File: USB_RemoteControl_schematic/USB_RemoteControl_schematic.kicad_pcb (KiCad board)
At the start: 2 copper layers, 82 x 20 mm, 33 parts, among them J1 USB_A, J2 FOUR_WIRE_CONN, SW1 ~rst, SW2 boot, U1 AMS1117-3.3, U2 STM32F103C6Tx, U3 NRF24L01_Breakout, Y1 8MHz

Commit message: Finished PCB
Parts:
- removed JP1: OPT_0, Resistor_SMD:R_0805_2012Metric_Pad1.20x1.40mm_HandSolder
- removed JP2: OPT_1, Resistor_SMD:R_0805_2012Metric_Pad1.20x1.40mm_HandSolder
- removed JP3: OPT_2, Resistor_SMD:R_0805_2012Metric_Pad1.20x1.40mm_HandSolder
- removed JP4: OPT_3, Resistor_SMD:R_0805_2012Metric_Pad1.20x1.40mm_HandSolder
- removed JP5: OPT_4, Resistor_SMD:R_0805_2012Metric_Pad1.20x1.40mm_HandSolder
- removed JP6: OPT_5, Resistor_SMD:R_0805_2012Metric_Pad1.20x1.40mm_HandSolder
- removed JP7: OPT_6, Resistor_SMD:R_0805_2012Metric_Pad1.20x1.40mm_HandSolder
- removed JP8: OPT_7, Resistor_SMD:R_0805_2012Metric_Pad1.20x1.40mm_HandSolder
- added D3: Green, LED_SMD:LED_0805_2012Metric_Pad1.15x1.40mm_HandSolder, F.Cu at (137.0, 118.3)
- added D4: Blue, LED_SMD:LED_0805_2012Metric_Pad1.15x1.40mm_HandSolder, F.Cu at (141.5, 118.3)
- added R7: 1K, Resistor_SMD:R_0805_2012Metric_Pad1.20x1.40mm_HandSolder, F.Cu at (134.8, 118.2)
- added R8: 1K, Resistor_SMD:R_0805_2012Metric_Pad1.20x1.40mm_HandSolder, F.Cu at (139.2, 118.2)
- added SW3: ~, custom_buttons_switches:TSB008, F.Cu at (135.2, 127.0)
- added SW4: ~, custom_buttons_switches:TSB008, F.Cu at (139.2, 127.0)
- C1, C2: footprint Capacitor_SMD:C_1206_3216Metric_Pad1.33x1.80mm_HandSolder -> Capacitor_SMD:C_0805_2012Metric_Pad1.18x1.45mm_HandSolder; moved to B.Cu
- C3, J2, R1, R2, R3, R5: moved to B.Cu
- D1, D2: footprint LED_SMD:LED_1206_3216Metric_Pad1.42x1.75mm_HandSolder -> LED_SMD:LED_0805_2012Metric_Pad1.15x1.40mm_HandSolder
- J1: footprint Connector_USB:USB_A_CONNFLY_DS1095-WNR0 -> Connectors_Custom:USB_A_Male
- R4: value 220R -> 1K; moved to B.Cu
- R6: value 220R -> 1K
- U1: value AMS1117-3.3 -> HT7533; footprint Package_TO_SOT_SMD:SOT-223-3_TabPin2 -> Package_TO_SOT_SMD:SOT-89-3; moved to B.Cu
- U3: value NRF24L01_Breakout -> JDY-33; footprint RF_Module:nRF24L01_Breakout -> Bluetooth_Custom:JDY-33, JDY-32, JDY-31, JDY-30, JDY-09
- Y1: footprint Crystal:Crystal_SMD_HC49-SD_HandSoldering -> Crystal:Crystal_SMD_HC49-SD
- moved SW2 81.1 mm to (130.8, 133.0), turned to 90 degrees
- moved C1 78.6 mm to (109.5, 129.0), turned to 270 degrees
- moved J2 77.2 mm to (111.0, 133.0), turned to 270 degrees
- moved R6 75.3 mm to (128.0, 118.2), turned to 270 degrees
- moved U1 73.1 mm to (113.5, 128.2), turned to 0 degrees
- moved J1 72.5 mm to (100.0, 125.0)
- moved R2 72.4 mm to (113.8, 122.3)
- moved SW1 71.5 mm to (131.2, 127.0)
- moved D2 71.5 mm to (130.2, 118.2), turned to 270 degrees
- moved R1 68.1 mm to (113.8, 120.0)
- moved C3 67.5 mm to (116.8, 124.8), turned to 0 degrees
- moved C2 66.7 mm to (110.5, 124.5), turned to 180 degrees
- moved C4 66.3 mm to (109.2, 128.9), turned to 270 degrees
- moved R3 65.3 mm to (119.0, 129.0)
- moved U3 62.5 mm to (132.5, 125.0), turned to 90 degrees
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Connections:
- D1 pad 1: Net-(D1-Pad1) -> GND
- D1 pad 2: /DBG_LED -> Net-(D1-Pad2)
- D2 pad 1: Net-(D2-Pad1) -> GND
- D2 pad 2: +3V3 -> Net-(D2-Pad2)
- R4 pad 1: Net-(D1-Pad1) -> /DBG_LED
- R4 pad 2: GND -> Net-(D1-Pad2)
- R6 pad 1: Net-(D2-Pad1) -> +3V3
- R6 pad 2: GND -> Net-(D2-Pad2)
- U1 pad 2: +3V3 -> +5V
- U1 pad 3: +5V -> +3V3
- U2 pad 10: /RF_IRQ -> /DBG_LED
- U2 pad 11: /RF_CE -> (no net)
- U2 pad 12: /~RF_CSN -> (no net)
- U2 pad 15: /SPI_SCK -> (no net)
- U2 pad 16: /SPI_MISO -> (no net)
- U2 pad 17: /SPI_MOSI -> (no net)
- U2 pad 2: /DBG_LED -> (no net)
- U2 pad 38: /OPT_0 -> (no net)
- U2 pad 39: /OPT_1 -> (no net)
- U2 pad 40: /OPT_2 -> (no net)
- U2 pad 41: /OPT_3 -> (no net)
- U2 pad 42: /OPT_4 -> /MCU_TX
- U2 pad 43: /OPT_5 -> /MCU_RX
- U2 pad 45: /OPT_6 -> (no net)
- U2 pad 46: /OPT_7 -> (no net)
- U3 pad 1: GND -> /MCU_RX
- U3 pad 2: +3V3 -> /MCU_TX
- U3 pad 3: /RF_CE -> (no net)
- U3 pad 4: /~RF_CSN -> (no net)
- U3 pad 5: /SPI_SCK -> (no net)
- U3 pad 6: /SPI_MOSI -> (no net)
- U3 pad 7: /SPI_MISO -> (no net)
- U3 pad 8: /RF_IRQ -> (no net)
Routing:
- net /MCU_RX: track 0.00 -> 36.1 mm, vias 0 -> 1
- net /MCU_TX: track 0.00 -> 35.0 mm, vias 0 -> 1
- net /SPI_MISO: track 28.2 -> 0.00 mm, vias 1 -> 0
- net /RF_CE: track 27.6 -> 0.00 mm, vias 2 -> 0
- net /SPI_SCK: track 27.4 -> 0.00 mm, vias 2 -> 0
- net /SPI_MOSI: track 25.3 -> 0.00 mm, vias 1 -> 0
- net /~RF_CSN: track 24.2 -> 0.00 mm, vias 2 -> 0
- net /RF_IRQ: track 23.8 -> 0.00 mm, vias 1 -> 0
- net /USBDM: track 33.9 -> 10.9 mm, vias 2 -> 1
- net +3V3: track 102.6 -> 80.9 mm, vias 0 -> 4
- net /OPT_0: track 20.9 -> 0.00 mm, vias 1 -> 0
- net GND: track 14.7 -> 34.4 mm, vias 7 -> 18
- net /USBDP: track 33.9 -> 14.3 mm, vias 2 -> 1
- net /OPT_1: track 18.6 -> 0.00 mm, vias 1 -> 0
- net /BT_RST: track 0.00 -> 18.2 mm, vias 0 -> 1
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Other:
- board size 82 x 20 mm -> 42 x 20 mm
- board text added: "boot"
- board text added: "bt aled"
- board text added: "bt en"
- board text added: "bt rst"
- board text added: "bt stat"
- board text added: "dbg"
- board text added: "pwr"
- board text added: "~rst"
- board text removed: "3v3"
- board text removed: "Gnd"
- board text removed: "JLCJLCJLCJLC"
- board text removed: "Option LSB"
- board text removed: "SWCLK"
- board text removed: "SWDIO"
- board text removed: "USB remote control v01 by MKrysz"

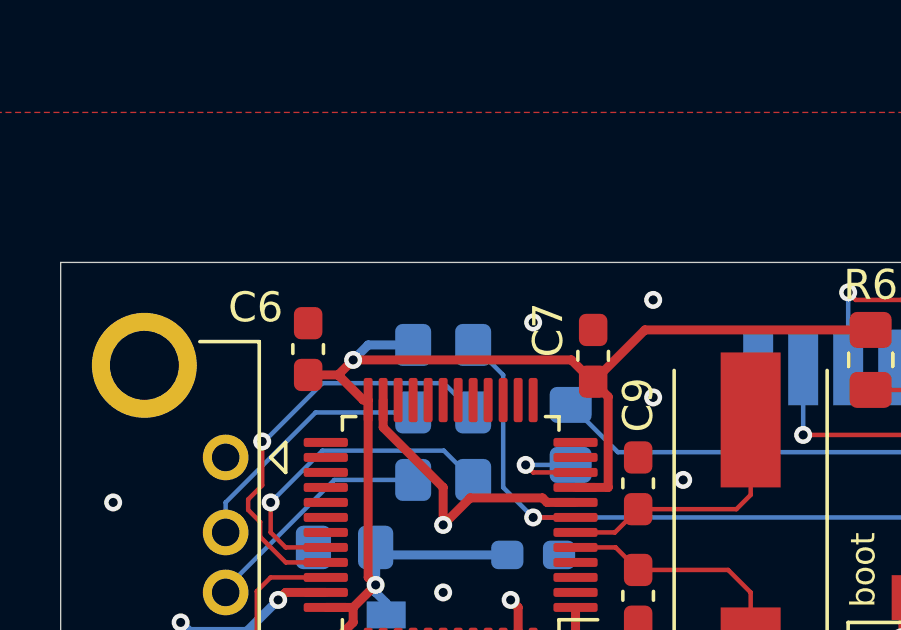
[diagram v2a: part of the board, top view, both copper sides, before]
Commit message: Added signature
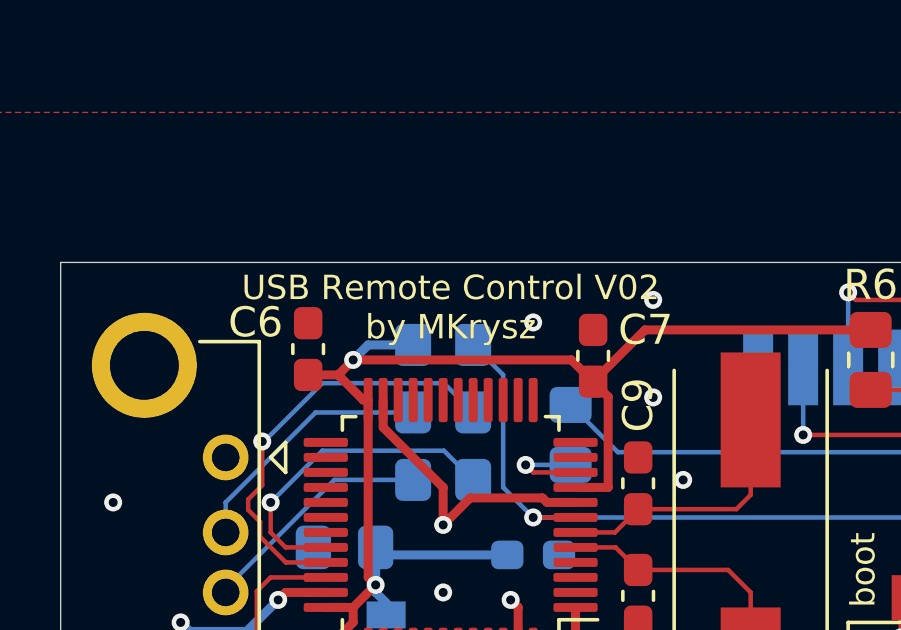
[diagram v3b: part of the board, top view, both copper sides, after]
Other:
- board text added: "USB Remote Control V02 by MKrysz"

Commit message: Generated new PCB's gerbers
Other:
- board text added: "JLCJLCJLCJLC"
